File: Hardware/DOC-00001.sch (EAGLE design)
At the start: 8 parts

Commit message: Routed. Needs ground layers.
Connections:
- net AIN0: now also JP1.5; no longer JP1.3
- net AIN1: now also JP1.6; no longer JP1.4
- net AIN2: now also JP1.7; no longer JP1.5
- net AIN3: now also JP1.8; no longer JP1.6
- net SCL: now also JP1.3; no longer JP1.7
- net SDA: now also JP1.4; no longer JP1.8
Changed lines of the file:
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@@
 </segment>
 <segment>
-<pinref part="JP1" gate="A" pin="7"/>
-<wire x1="134.62" y1="0" x2="119.38" y2="0" width="0.1524" layer="91"/>
-<label x="119.38" y="0" size="1.778" layer="95"/>
+<pinref part="JP1" gate="A" pin="3"/>
+<wire x1="134.62" y1="10.16" x2="119.38" y2="10.16" width="0.1524" layer="91"/>
+<label x="119.38" y="10.16" size="1.778" layer="95"/>
 </segment>
 </net>
@@
 </segment>
 <segment>
-<pinref part="JP1" gate="A" pin="8"/>
-<wire x1="134.62" y1="-2.54" x2="119.38" y2="-2.54" width="0.1524" layer="91"/>
-<label x="119.38" y="-2.54" size="1.778" layer="95"/>
+<pinref part="JP1" gate="A" pin="4"/>
+<wire x1="134.62" y1="7.62" x2="119.38" y2="7.62" width="0.1524" layer="91"/>
+<label x="119.38" y="7.62" size="1.778" layer="95"/>
 </segment>
 </net>
@@
 </segment>
 <segment>
-<pinref part="JP1" gate="A" pin="3"/>
-<wire x1="134.62" y1="10.16" x2="119.38" y2="10.16" width="0.1524" layer="91"/>
-<label x="119.38" y="10.16" size="1.778" layer="95"/>
+<pinref part="JP1" gate="A" pin="5"/>
+<wire x1="134.62" y1="5.08" x2="119.38" y2="5.08" width="0.1524" layer="91"/>
+<label x="119.38" y="5.08" size="1.778" layer="95"/>
 </segment>
 </net>
@@
 </segment>
 <segment>
-<pinref part="JP1" gate="A" pin="4"/>
-<wire x1="134.62" y1="7.62" x2="119.38" y2="7.62" width="0.1524" layer="91"/>
-<label x="119.38" y="7.62" size="1.778" layer="95"/>
+<pinref part="JP1" gate="A" pin="6"/>
+<wire x1="134.62" y1="2.54" x2="119.38" y2="2.54" width="0.1524" layer="91"/>
+<label x="119.38" y="2.54" size="1.778" layer="95"/>
 </segment>
 </net>
@@
 </segment>
 <segment>
-<pinref part="JP1" gate="A" pin="5"/>
-<wire x1="134.62" y1="5.08" x2="119.38" y2="5.08" width="0.1524" layer="91"/>
-<label x="119.38" y="5.08" size="1.778" layer="95"/>
+<pinref part="JP1" gate="A" pin="7"/>
+<wire x1="134.62" y1="0" x2="119.38" y2="0" width="0.1524" layer="91"/>
+<label x="119.38" y="0" size="1.778" layer="95"/>
 </segment>
 </net>
@@
 </segment>
 <segment>
-<pinref part="JP1" gate="A" pin="6"/>
-<wire x1="134.62" y1="2.54" x2="119.38" y2="2.54" width="0.1524" layer="91"/>
-<label x="119.38" y="2.54" size="1.778" layer="95"/>
+<pinref part="JP1" gate="A" pin="8"/>
+<wire x1="134.62" y1="-2.54" x2="119.38" y2="-2.54" width="0.1524" layer="91"/>
+<label x="119.38" y="-2.54" size="1.778" layer="95"/>
 </segment>
 </net>

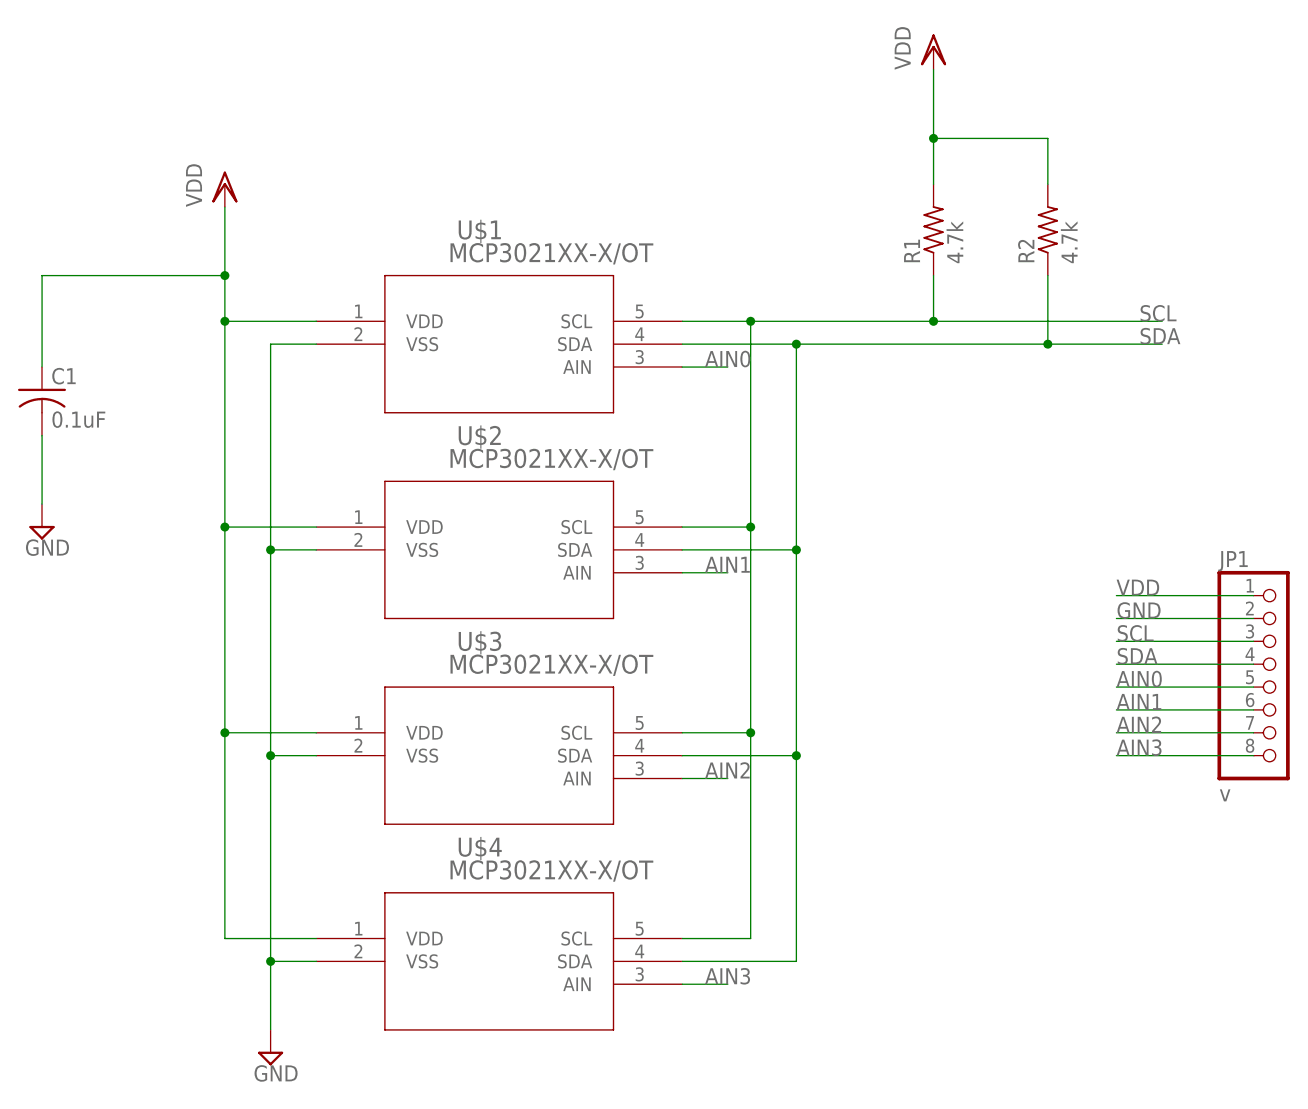
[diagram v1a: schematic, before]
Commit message: Added BOM.
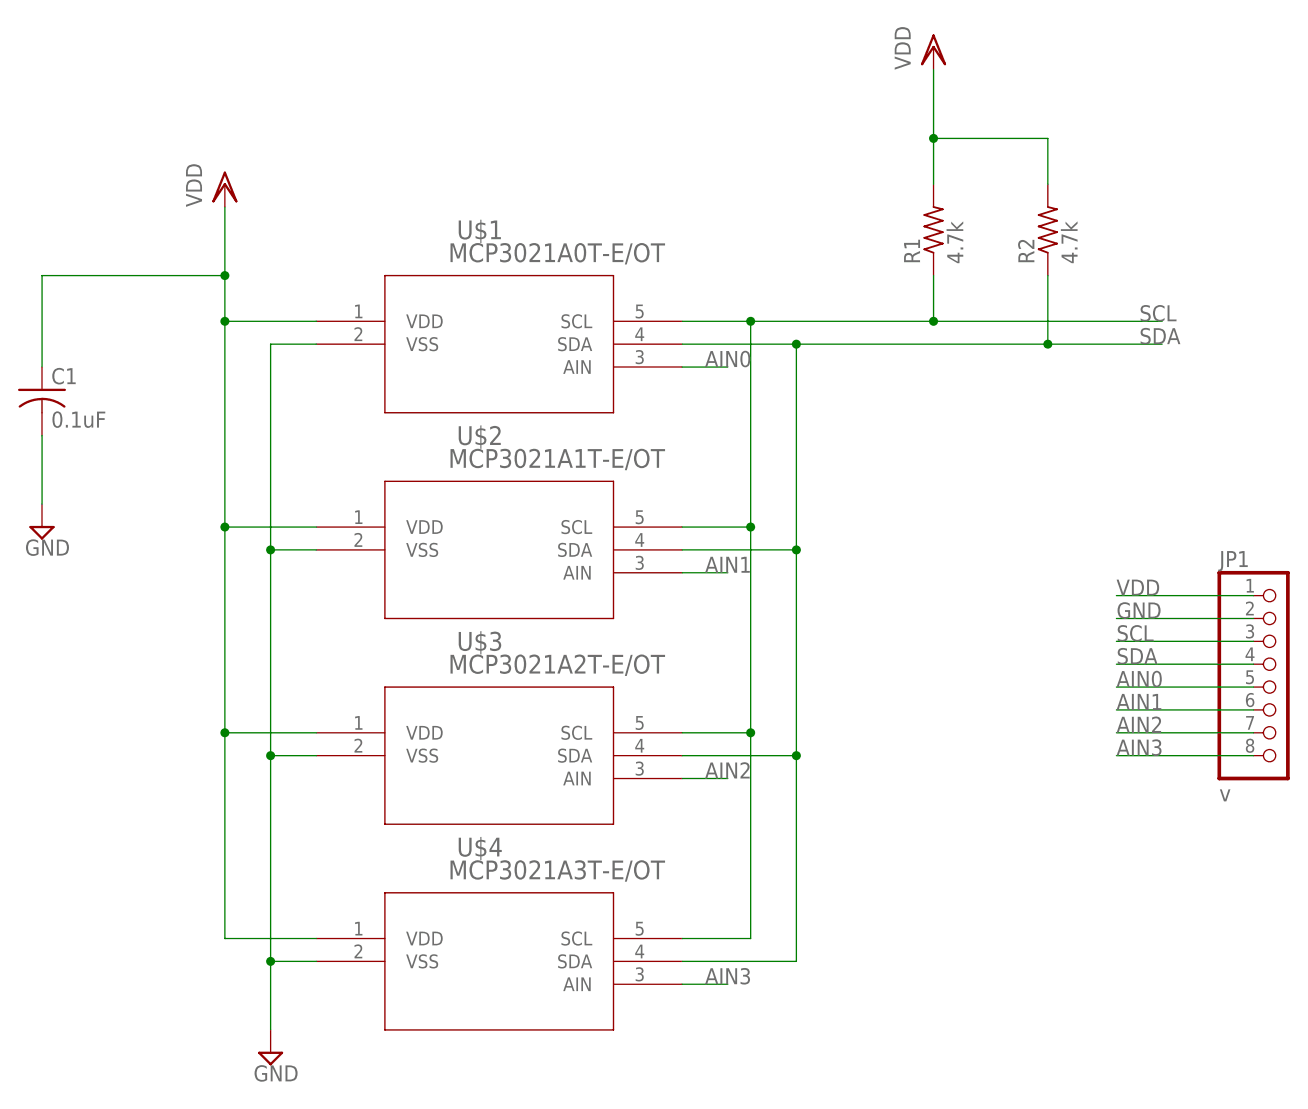
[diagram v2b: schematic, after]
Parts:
- C1: MPN (none) -> VJ0805Y104MXXAC; PRICE (none) -> 0.06; STORE (none) -> mouser.com
- JP1: MPN (none) -> 825433-8; PRICE (none) -> 0.84; STORE (none) -> mouser.com
- R1, R2: MPN (none) -> CRCW08054K70FKEA; PRICE (none) -> 0.08; STORE (none) -> mouser.com
- U$1: value MCP3021XX-X/OT -> MCP3021A0T-E/OT; MPN (none) -> MCP3021A0T-E/OT; PRICE (none) -> 1.07; STORE (none) -> microchipdirect.com
- U$2: value MCP3021XX-X/OT -> MCP3021A1T-E/OT; MPN (none) -> MCP3021A1T-E/OT; PRICE (none) -> 1.07; STORE (none) -> microchipdirect.com
- U$3: value MCP3021XX-X/OT -> MCP3021A2T-E/OT; MPN (none) -> MCP3021A2T-E/OT; PRICE (none) -> 1.07; STORE (none) -> microchipdirect.com
- U$4: value MCP3021XX-X/OT -> MCP3021A3T-E/OT; MPN (none) -> MCP3021A3T-E/OT; PRICE (none) -> 1.07; STORE (none) -> microchipdirect.com

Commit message: Fixed values of Ux in sch to match PCBs, there was a space after the value name so I just deleted that. Added cost sheet.
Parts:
- U$1: value MCP3021A0T-E/OT -> MCP3021A0T-E/OT
- U$2: value MCP3021A1T-E/OT -> MCP3021A1T-E/OT
- U$3: value MCP3021A2T-E/OT -> MCP3021A2T-E/OT
- U$4: value MCP3021A3T-E/OT -> MCP3021A3T-E/OT
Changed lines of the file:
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@@
 <grid distance="0.1" unitdist="inch" unit="inch" style="lines" multiple="1" display="no" altdistance="0.01" altunitdist="inch" altunit="inch"/>
 <layers>
-<layer number="1" name="Top" color="4" fill="1" visible="yes" active="no"/>
-<layer number="2" name="Route2" color="1" fill="3" visible="yes" active="no"/>
-<layer number="3" name="Route3" color="4" fill="3" visible="yes" active="no"/>
-<layer number="4" name="Route4" color="1" fill="4" visible="yes" active="no"/>
-<layer number="5" name="Route5" color="4" fill="4" visible="yes" active="no"/>
-<layer number="6" name="Route6" color="1" fill="8" visible="yes" active="no"/>
-<layer number="7" name="Route7" color="4" fill="8" visible="yes" active="no"/>
-<layer number="8" name="Route8" color="1" fill="2" visible="yes" active="no"/>
-<layer number="9" name="Route9" color="4" fill="2" visible="yes" active="no"/>
-<layer number="10" name="Route10" color="1" fill="7" visible="yes" active="no"/>
-<layer number="11" name="Route11" color="4" fill="7" visible="yes" active="no"/>
-<layer number="12" name="Route12" color="1" fill="5" visible="yes" active="no"/>
-<layer number="13" name="Route13" color="4" fill="5" visible="yes" active="no"/>
-<layer number="14" name="Route14" color="1" fill="6" visible="yes" active="no"/>
-<layer number="15" name="Route15" color="4" fill="6" visible="yes" active="no"/>
-<layer number="16" name="Bottom" color="1" fill="1" visible="yes" active="no"/>
-<layer number="17" name="Pads" color="2" fill="1" visible="yes" active="no"/>
-<layer number="18" name="Vias" color="2" fill="1" visible="yes" active="no"/>
-<layer number="19" name="Unrouted" color="6" fill="1" visible="yes" active="no"/>
-<layer number="20" name="Dimension" color="15" fill="1" visible="yes" active="no"/>
-<layer number="21" name="tPlace" color="7" fill="1" visible="yes" active="no"/>
-<layer number="22" name="bPlace" color="7" fill="1" visible="yes" active="no"/>
-<layer number="23" name="tOrigins" color="15" fill="1" visible="yes" active="no"/>
-<layer number="24" name="bOrigins" color="15" fill="1" visible="yes" active="no"/>
-<layer number="25" name="tNames" color="7" fill="1" visible="yes" active="no"/>
-<layer number="26" name="bNames" color="7" fill="1" visible="yes" active="no"/>
-<layer number="27" name="tValues" color="7" fill="1" visible="yes" active="no"/>
-<layer number="28" name="bValues" color="7" fill="1" visible="yes" active="no"/>
+<layer number="1" name="Top" color="4" fill="1" visible="no" active="no"/>
+<layer number="2" name="Route2" color="1" fill="3" visible="no" active="no"/>
+<layer number="3" name="Route3" color="4" fill="3" visible="no" active="no"/>
+<layer number="4" name="Route4" color="1" fill="4" visible="no" active="no"/>
+<layer number="5" name="Route5" color="4" fill="4" visible="no" active="no"/>
+<layer number="6" name="Route6" color="1" fill="8" visible="no" active="no"/>
+<layer number="7" name="Route7" color="4" fill="8" visible="no" active="no"/>
+<layer number="8" name="Route8" color="1" fill="2" visible="no" active="no"/>
+<layer number="9" name="Route9" color="4" fill="2" visible="no" active="no"/>
+<layer number="10" name="Route10" color="1" fill="7" visible="no" active="no"/>
+<layer number="11" name="Route11" color="4" fill="7" visible="no" active="no"/>
+<layer number="12" name="Route12" color="1" fill="5" visible="no" active="no"/>
+<layer number="13" name="Route13" color="4" fill="5" visible="no" active="no"/>
+<layer number="14" name="Route14" color="1" fill="6" visible="no" active="no"/>
+<layer number="15" name="Route15" color="4" fill="6" visible="no" active="no"/>
+<layer number="16" name="Bottom" color="1" fill="1" visible="no" active="no"/>
+<layer number="17" name="Pads" color="2" fill="1" visible="no" active="no"/>
+<layer number="18" name="Vias" color="2" fill="1" visible="no" active="no"/>
+<layer number="19" name="Unrouted" color="6" fill="1" visible="no" active="no"/>
+<layer number="20" name="Dimension" color="15" fill="1" visible="no" active="no"/>
+<layer number="21" name="tPlace" color="7" fill="1" visible="no" active="no"/>
+<layer number="22" name="bPlace" color="7" fill="1" visible="no" active="no"/>
+<layer number="23" name="tOrigins" color="15" fill="1" visible="no" active="no"/>
+<layer number="24" name="bOrigins" color="15" fill="1" visible="no" active="no"/>
+<layer number="25" name="tNames" color="7" fill="1" visible="no" active="no"/>
+<layer number="26" name="bNames" color="7" fill="1" visible="no" active="no"/>
+<layer number="27" name="tValues" color="7" fill="1" visible="no" active="no"/>
+<layer number="28" name="bValues" color="7" fill="1" visible="no" active="no"/>
 <layer number="29" name="tStop" color="7" fill="3" visible="no" active="no"/>
 <layer number="30" name="bStop" color="7" fill="6" visible="no" active="no"/>
@@
 <layer number="35" name="tGlue" color="7" fill="4" visible="no" active="no"/>
 <layer number="36" name="bGlue" color="7" fill="5" visible="no" active="no"/>
-<layer number="37" name="tTest" color="7" fill="1" visible="yes" active="no"/>
-<layer number="38" name="bTest" color="7" fill="1" visible="yes" active="no"/>
+<layer number="37" name="tTest" color="7" fill="1" visible="no" active="no"/>
+<layer number="38" name="bTest" color="7" fill="1" visible="no" active="no"/>
 <layer number="39" name="tKeepout" color="4" fill="11" visible="no" active="no"/>
 <layer number="40" name="bKeepout" color="1" fill="11" visible="no" active="no"/>
@@
 <layer number="44" name="Drills" color="7" fill="1" visible="no" active="no"/>
 <layer number="45" name="Holes" color="7" fill="1" visible="no" active="no"/>
-<layer number="46" name="Milling" color="3" fill="1" visible="yes" active="no"/>
-<layer number="47" name="Measures" color="7" fill="1" visible="yes" active="no"/>
-<layer number="48" name="Document" color="7" fill="1" visible="yes" active="no"/>
-<layer number="49" name="Reference" color="7" fill="1" visible="yes" active="no"/>
-<layer number="51" name="tDocu" color="7" fill="1" visible="yes" active="no"/>
-<layer number="52" name="bDocu" color="7" fill="1" visible="yes" active="no"/>
+<layer number="46" name="Milling" color="3" fill="1" visible="no" active="no"/>
+<layer number="47" name="Measures" color="7" fill="1" visible="no" active="no"/>
+<layer number="48" name="Document" color="7" fill="1" visible="no" active="no"/>
+<layer number="49" name="Reference" color="7" fill="1" visible="no" active="no"/>
+<layer number="51" name="tDocu" color="7" fill="1" visible="no" active="no"/>
+<layer number="52" name="bDocu" color="7" fill="1" visible="no" active="no"/>
 <layer number="91" name="Nets" color="2" fill="1" visible="yes" active="yes"/>
 <layer number="92" name="Busses" color="1" fill="1" visible="yes" active="yes"/>
@@
 </classes>
 <parts>
-<part name="U$1" library="MCP3021AX" deviceset="MCP3021XX-X/OT" device="" value="MCP3021A0T-E/OT ">
+<part name="U$1" library="MCP3021AX" deviceset="MCP3021XX-X/OT" device="" value="MCP3021A0T-E/OT">
 <attribute name="MPN" value="MCP3021A0T-E/OT"/>
 <attribute name="PRICE" value="1.07"/>
 <attribute name="STORE" value="microchipdirect.com"/>
 </part>
-<part name="U$2" library="MCP3021AX" deviceset="MCP3021XX-X/OT" device="" value="MCP3021A1T-E/OT ">
+<part name="U$2" library="MCP3021AX" deviceset="MCP3021XX-X/OT" device="" value="MCP3021A1T-E/OT">
 <attribute name="MPN" value="MCP3021A1T-E/OT"/>
 <attribute name="PRICE" value="1.07"/>
 <attribute name="STORE" value="microchipdirect.com"/>
 </part>
-<part name="U$3" library="MCP3021AX" deviceset="MCP3021XX-X/OT" device="" value="MCP3021A2T-E/OT ">
+<part name="U$3" library="MCP3021AX" deviceset="MCP3021XX-X/OT" device="" value="MCP3021A2T-E/OT">
 <attribute name="MPN" value="MCP3021A2T-E/OT"/>
 <attribute name="PRICE" value="1.07"/>
 <attribute name="STORE" value="microchipdirect.com"/>
 </part>
-<part name="U$4" library="MCP3021AX" deviceset="MCP3021XX-X/OT" device="" value="MCP3021A3T-E/OT ">
+<part name="U$4" library="MCP3021AX" deviceset="MCP3021XX-X/OT" device="" value="MCP3021A3T-E/OT">
 <attribute name="MPN" value="MCP3021A3T-E/OT"/>
 <attribute name="PRICE" value="1.07"/>
